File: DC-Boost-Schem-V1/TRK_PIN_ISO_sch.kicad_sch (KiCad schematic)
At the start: 10 parts, among them Q9 HCNR200-300E, U20 MCP6007, U21 MCP6007

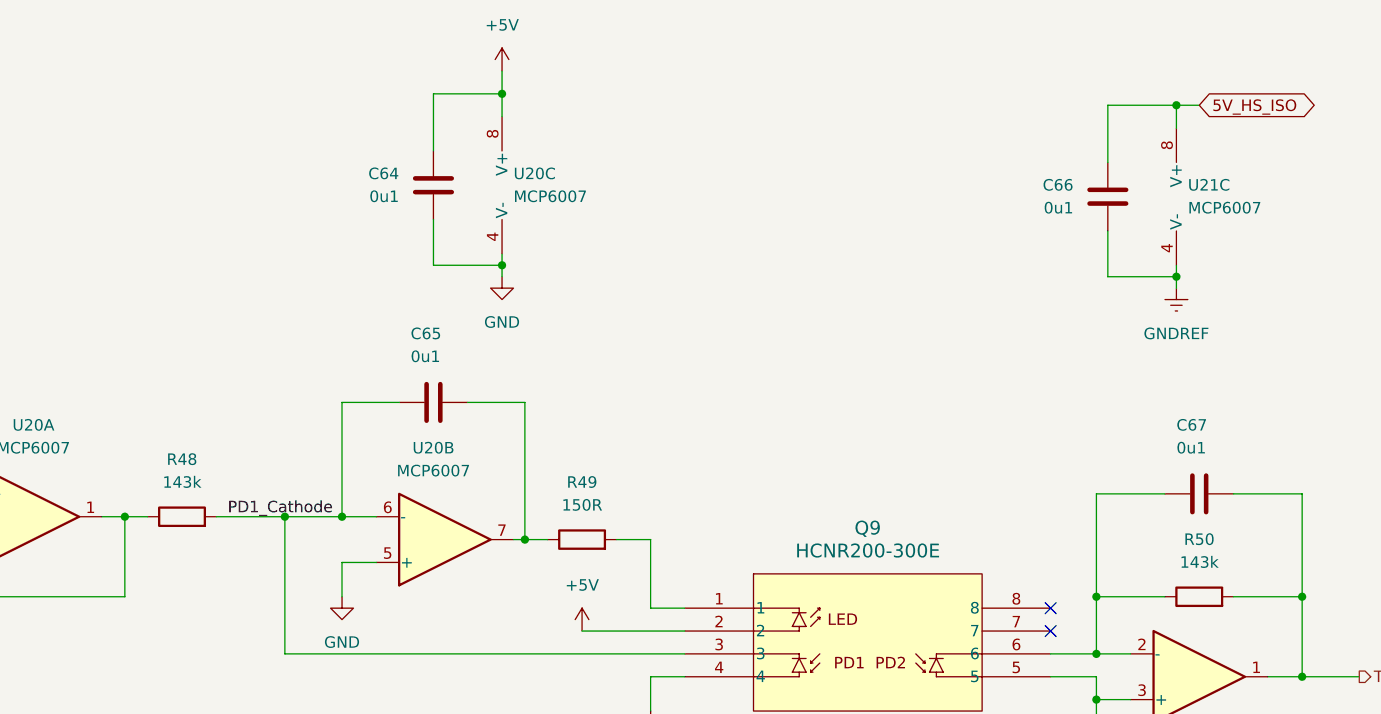
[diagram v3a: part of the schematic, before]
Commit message: More layout and routing
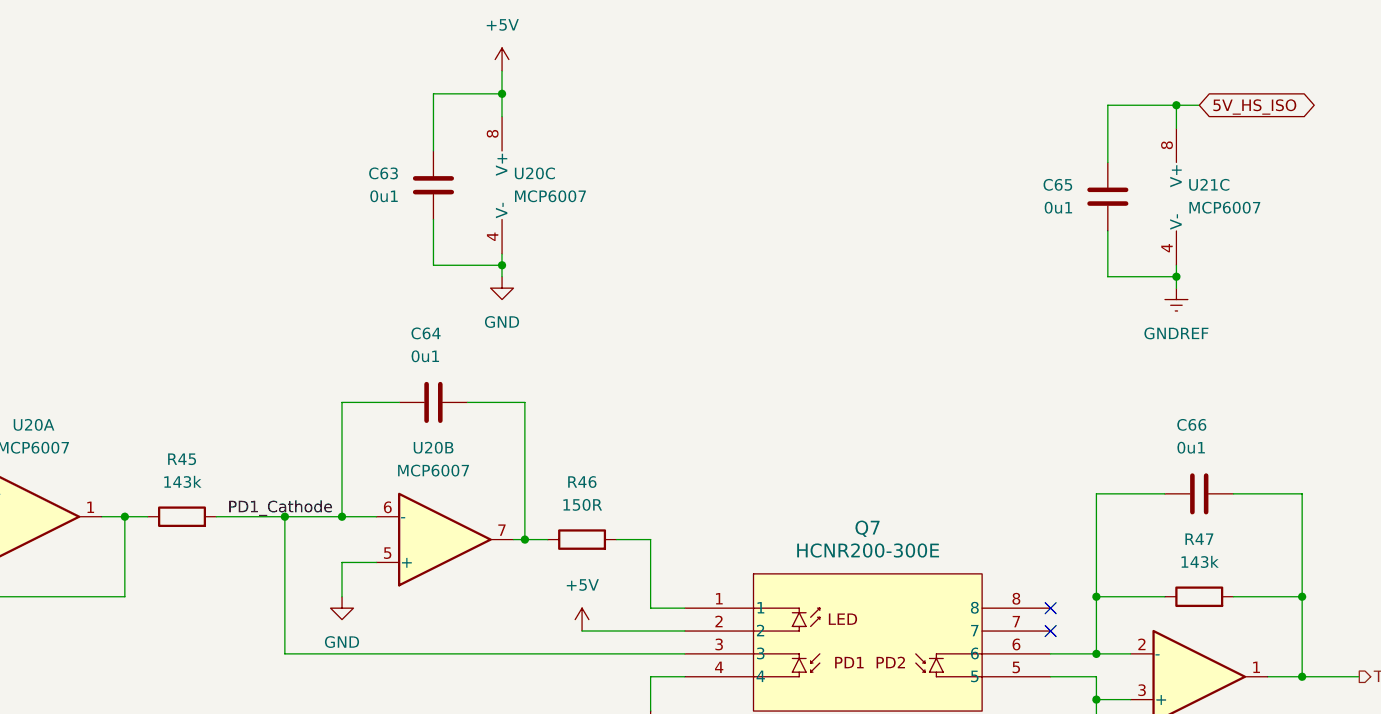
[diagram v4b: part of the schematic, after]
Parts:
- renumbered C64 to C63, C65 to C64, C66 to C65, C67 to C66, Q9 to Q7, R48 to R45, R49 to R46, R50 to R47
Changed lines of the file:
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@@
+		(dnp no)
+		(fields_autoplaced yes)
+		(property "Reference" "#PWR084"
+			(at 110.49 119.38 0)
+			(effects
+				(font
+					(size 1.27 1.27)
+				)
+				(hide yes)
+			)
+		)
+		(property "Value" "GND"
+			(at 110.49 118.11 0)
+			(effects
+				(font
+					(size 1.27 1.27)
+				)
+			)
+		)
+		(property "Footprint" ""
+			(at 110.49 113.03 0)
+			(effects
+				(font
+					(size 1.27 1.27)
+				)
+				(hide yes)
+			)
+		)
+		(property "Datasheet" ""
+			(at 110.49 113.03 0)
+			(effects
+				(font
+					(size 1.27 1.27)
+				)
+				(hide yes)
+			)
+		)
+		(property "Description" "Power symbol creates a global label with name \"GND\" , ground"
+			(at 110.49 113.03 0)
+			(effects
+				(font
+					(size 1.27 1.27)
+				)
+				(hide yes)
+			)
+		)
+		(pin "1"
+		)
+		(instances
+			(project "DC-DC-Boost-V1"
+				(path "/892bc44b-f7f8-4677-bf53-06d5523b6450/83854842-4c14-4e3d-b9f8-9c4b216ba0c1"
+					(reference "#PWR084")
+					(unit 1)
+				)
+			)
+		)
+	)
+	(symbol
+		(lib_id "power:GNDREF")
+		(at 203.2 78.74 0)
+		(unit 1)
+		(exclude_from_sim no)
+		(in_bom yes)
+		(on_board yes)
+		(dnp no)
+		(fields_autoplaced yes)
+		(property "Reference" "#PWR090"
+			(at 203.2 85.09 0)
+			(effects
+				(font
+					(size 1.27 1.27)
+				)
+				(hide yes)
+			)
+		)
+		(property "Value" "GNDREF"
+			(at 203.2 83.82 0)
+			(effects
+				(font
+					(size 1.27 1.27)
+				)
+			)
+		)
+		(property "Footprint" ""
+			(at 203.2 78.74 0)
+			(effects
+				(font
+					(size 1.27 1.27)
+				)
+				(hide yes)
+			)
+		)
+		(property "Datasheet" ""
+			(at 203.2 78.74 0)
+			(effects
+				(font
+					(size 1.27 1.27)
+				)
+				(hide yes)
+			)
+		)
+		(property "Description" "Power symbol creates a global label with name \"GNDREF\" , reference supply ground"
+			(at 203.2 78.74 0)
+			(effects
+				(font
+					(size 1.27 1.27)
+				)
+				(hide yes)
+			)
+		)
+		(pin "1"
+		)
+		(instances
+			(project "DC-DC-Boost-V1"
+				(path "/892bc44b-f7f8-4677-bf53-06d5523b6450/83854842-4c14-4e3d-b9f8-9c4b216ba0c1"
+					(reference "#PWR090")
+					(unit 1)
+				)
+			)
+		)
+	)
+	(symbol
+		(lib_id "power:GNDREF")
+		(at 194.31 129.54 0)
+		(unit 1)
+		(exclude_from_sim no)
+		(in_bom yes)
+		(on_board yes)
 		(dnp no)
 		(fields_autoplaced yes)
 		(property "Reference" "#PWR089"
-			(at 110.49 119.38 0)
-			(effects
-				(font
-					(size 1.27 1.27)
-				)
-				(hide yes)
-			)
-		)
-		(property "Value" "GND"
-			(at 110.49 118.11 0)
-			(effects
-				(font
-					(size 1.27 1.27)
-				)
-			)
-		)
-		(property "Footprint" ""
-			(at 110.49 113.03 0)
-			(effects
-				(font
-					(size 1.27 1.27)
-				)
-				(hide yes)
-			)
-		)
-		(property "Datasheet" ""
-			(at 110.49 113.03 0)
-			(effects
-				(font
-					(size 1.27 1.27)
-				)
-				(hide yes)
-			)
-		)
-		(property "Description" "Power symbol creates a global label with name \"GND\" , ground"
-			(at 110.49 113.03 0)
-			(effects
-				(font
-					(size 1.27 1.27)
-				)
-				(hide yes)
-			)
-		)
-		(pin "1"
-		)
-		(instances
-			(project "DC-DC-Boost-V1"
-				(path "/892bc44b-f7f8-4677-bf53-06d5523b6450/83854842-4c14-4e3d-b9f8-9c4b216ba0c1"
-					(reference "#PWR089")
-					(unit 1)
-				)
-			)
-		)
-	)
-	(symbol
-		(lib_id "power:GNDREF")
-		(at 203.2 78.74 0)
-		(unit 1)
-		(exclude_from_sim no)
-		(in_bom yes)
-		(on_board yes)
-		(dnp no)
-		(fields_autoplaced yes)
-		(property "Reference" "#PWR0601"
-			(at 203.2 85.09 0)
-			(effects
-				(font
-					(size 1.27 1.27)
-				)
-				(hide yes)
-			)
-		)
-		(property "Value" "GNDREF"
-			(at 203.2 83.82 0)
-			(effects
-				(font
-					(size 1.27 1.27)
-				)
-			)
-		)
-		(property "Footprint" ""
-			(at 203.2 78.74 0)
-			(effects
-				(font
-					(size 1.27 1.27)
-				)
-				(hide yes)
-			)
-		)
-		(property "Datasheet" ""
-			(at 203.2 78.74 0)
-			(effects
-				(font
-					(size 1.27 1.27)
-				)
-				(hide yes)
-			)
-		)
-		(property "Description" "Power symbol creates a global label with name \"GNDREF\" , reference supply ground"
-			(at 203.2 78.74 0)
-			(effects
-				(font
-					(size 1.27 1.27)
-				)
-				(hide yes)
-			)
-		)
-		(pin "1"
-		)
-		(instances
-			(project "DC-DC-Boost-V1"
-				(path "/892bc44b-f7f8-4677-bf53-06d5523b6450/83854842-4c14-4e3d-b9f8-9c4b216ba0c1"
-					(reference "#PWR0601")
-					(unit 1)
-				)
-			)
-		)
-	)
-	(symbol
-		(lib_id "power:GNDREF")
-		(at 194.31 129.54 0)
-		(unit 1)
-		(exclude_from_sim no)
-		(in_bom yes)
-		(on_board yes)
-		(dnp no)
-		(fields_autoplaced yes)
-		(property "Reference" "#PWR0602"
 			(at 194.31 135.89 0)
 			(effects
@@
 			(project "DC-DC-Boost-V1"
 				(path "/892bc44b-f7f8-4677-bf53-06d5523b6450/83854842-4c14-4e3d-b9f8-9c4b216ba0c1"
-					(reference "#PWR0602")
+					(reference "#PWR089")
 					(unit 1)
 				)
@@
 		(dnp no)
 		(fields_autoplaced yes)
-		(property "Reference" "R50"
+		(property "Reference" "R47"
 			(at 205.74 106.68 90)
 			(effects
@@
 			(project "DC-DC-Boost-V1"
 				(path "/892bc44b-f7f8-4677-bf53-06d5523b6450/83854842-4c14-4e3d-b9f8-9c4b216ba0c1"
-					(reference "R50")
+					(reference "R47")
 					(unit 1)
 				)
@@
 		(dnp no)
 		(fields_autoplaced yes)
-		(property "Reference" "#PWR090"
+		(property "Reference" "#PWR086"
 			(at 128.27 83.82 0)
 			(effects
@@
 			(project "DC-DC-Boost-V1"
 				(path "/892bc44b-f7f8-4677-bf53-06d5523b6450/83854842-4c14-4e3d-b9f8-9c4b216ba0c1"
-					(reference "#PWR090")
+					(reference "#PWR086")
 					(unit 1)
 				)
@@
 		(on_board yes)
 		(dnp no)
-		(property "Reference" "C64"
+		(property "Reference" "C63"
 			(at 116.84 66.04 0)
 			(effects
@@
 			(project "DC-DC-Boost-V1"
 				(path "/892bc44b-f7f8-4677-bf53-06d5523b6450/83854842-4c14-4e3d-b9f8-9c4b216ba0c1"
-					(reference "C64")
+					(reference "C63")
 					(unit 1)
 				)
@@
 		(on_board yes)
 		(dnp no)
-		(property "Reference" "C67"
+		(property "Reference" "C66"
 			(at 203.2 93.98 90)
 			(effects
@@
 			(project "DC-DC-Boost-V1"
 				(path "/892bc44b-f7f8-4677-bf53-06d5523b6450/83854842-4c14-4e3d-b9f8-9c4b216ba0c1"
-					(reference "C67")
+					(reference "C66")
 					(unit 1)
 				)
@@
 		(dnp no)
 		(fields_autoplaced yes)
-		(property "Reference" "R48"
+		(property "Reference" "R45"
 			(at 92.71 97.79 90)
 			(effects
@@
 			(project "DC-DC-Boost-V1"
 				(path "/892bc44b-f7f8-4677-bf53-06d5523b6450/83854842-4c14-4e3d-b9f8-9c4b216ba0c1"
-					(reference "R48")
+					(reference "R45")
 					(unit 1)
 				)
@@
 		(dnp no)
 		(fields_autoplaced yes)
-		(property "Reference" "#PWR093"
+		(property "Reference" "#PWR088"
 			(at 144.78 132.08 0)
 			(effects
@@
 			(project "DC-DC-Boost-V1"
 				(path "/892bc44b-f7f8-4677-bf53-06d5523b6450/83854842-4c14-4e3d-b9f8-9c4b216ba0c1"
-					(reference "#PWR093")
+					(reference "#PWR088")
 					(unit 1)
 				)
@@
 		(dnp no)
 		(fields_autoplaced yes)
-		(property "Reference" "#PWR092"
+		(property "Reference" "#PWR087"
 			(at 137.16 120.65 0)
 			(effects
@@
 			(project "DC-DC-Boost-V1"
 				(path "/892bc44b-f7f8-4677-bf53-06d5523b6450/83854842-4c14-4e3d-b9f8-9c4b216ba0c1"
-					(reference "#PWR092")
+					(reference "#PWR087")
 					(unit 1)
 				)
@@
 		(on_board yes)
 		(dnp no)
-		(property "Reference" "Q9"
+		(property "Reference" "Q7"
 			(at 168.91 105.41 0)
 			(effects
@@
 			(project "DC-DC-Boost-V1"
 				(path "/892bc44b-f7f8-4677-bf53-06d5523b6450/83854842-4c14-4e3d-b9f8-9c4b216ba0c1"
-					(reference "Q9")
+					(reference "Q7")
 					(unit 1)
 				)
@@
 		(dnp no)
 		(fields_autoplaced yes)
-		(property "Reference" "R49"
+		(property "Reference" "R46"
 			(at 137.16 100.33 90)
 			(effects
@@
 			(project "DC-DC-Boost-V1"
 				(path "/892bc44b-f7f8-4677-bf53-06d5523b6450/83854842-4c14-4e3d-b9f8-9c4b216ba0c1"
-					(reference "R49")
+					(reference "R46")
 					(unit 1)
 				)
@@
 		(dnp no)
 		(fields_autoplaced yes)
-		(property "Reference" "#PWR091"
+		(property "Reference" "#PWR085"
 			(at 128.27 58.42 0)
 			(effects
@@
 			(project "DC-DC-Boost-V1"
 				(path "/892bc44b-f7f8-4677-bf53-06d5523b6450/83854842-4c14-4e3d-b9f8-9c4b216ba0c1"
-					(reference "#PWR091")
+					(reference "#PWR085")
 					(unit 1)
 				)
@@
 		(on_board yes)
 		(dnp no)
-		(property "Reference" "C65"
+		(property "Reference" "C64"
 			(at 118.11 83.82 90)
 			(effects
@@
 			(project "DC-DC-Boost-V1"
 				(path "/892bc44b-f7f8-4677-bf53-06d5523b6450/83854842-4c14-4e3d-b9f8-9c4b216ba0c1"
-					(reference "C65")
+					(reference "C64")
 					(unit 1)
 				)
@@
 		(on_board yes)
 		(dnp no)
-		(property "Reference" "C66"
+		(property "Reference" "C65"
 			(at 191.77 67.31 0)
 			(effects
@@
 			(project "DC-DC-Boost-V1"
 				(path "/892bc44b-f7f8-4677-bf53-06d5523b6450/83854842-4c14-4e3d-b9f8-9c4b216ba0c1"
-					(reference "C66")
-					(unit 1)
-				)
+					(reference "C65")
+					(unit 1)
+				)

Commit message: Added more to layout
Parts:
- renumbered C63 to C66, C64 to C67, C65 to C68, C66 to C69, R45 to R47, R46 to R48, R47 to R49
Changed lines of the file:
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@@
 		(dnp no)
 		(fields_autoplaced yes)
-		(property "Reference" "R47"
+		(property "Reference" "R49"
 			(at 205.74 106.68 90)
 			(effects
@@
 			(project "DC-DC-Boost-V1"
 				(path "/892bc44b-f7f8-4677-bf53-06d5523b6450/83854842-4c14-4e3d-b9f8-9c4b216ba0c1"
-					(reference "R47")
+					(reference "R49")
 					(unit 1)
 				)
@@
 		(on_board yes)
 		(dnp no)
-		(property "Reference" "C63"
+		(property "Reference" "C66"
 			(at 116.84 66.04 0)
 			(effects
@@
 			(project "DC-DC-Boost-V1"
 				(path "/892bc44b-f7f8-4677-bf53-06d5523b6450/83854842-4c14-4e3d-b9f8-9c4b216ba0c1"
-					(reference "C63")
+					(reference "C66")
 					(unit 1)
 				)
@@
 		(on_board yes)
 		(dnp no)
-		(property "Reference" "C66"
+		(property "Reference" "C69"
 			(at 203.2 93.98 90)
 			(effects
@@
 			(project "DC-DC-Boost-V1"
 				(path "/892bc44b-f7f8-4677-bf53-06d5523b6450/83854842-4c14-4e3d-b9f8-9c4b216ba0c1"
-					(reference "C66")
+					(reference "C69")
 					(unit 1)
 				)
@@
 		(dnp no)
 		(fields_autoplaced yes)
-		(property "Reference" "R45"
+		(property "Reference" "R47"
 			(at 92.71 97.79 90)
 			(effects
@@
 			(project "DC-DC-Boost-V1"
 				(path "/892bc44b-f7f8-4677-bf53-06d5523b6450/83854842-4c14-4e3d-b9f8-9c4b216ba0c1"
-					(reference "R45")
+					(reference "R47")
 					(unit 1)
 				)
@@
 		(dnp no)
 		(fields_autoplaced yes)
-		(property "Reference" "R46"
+		(property "Reference" "R48"
 			(at 137.16 100.33 90)
 			(effects
@@
 			(project "DC-DC-Boost-V1"
 				(path "/892bc44b-f7f8-4677-bf53-06d5523b6450/83854842-4c14-4e3d-b9f8-9c4b216ba0c1"
-					(reference "R46")
+					(reference "R48")
 					(unit 1)
 				)
@@
 		(on_board yes)
 		(dnp no)
-		(property "Reference" "C64"
+		(property "Reference" "C67"
 			(at 118.11 83.82 90)
 			(effects
@@
 			(project "DC-DC-Boost-V1"
 				(path "/892bc44b-f7f8-4677-bf53-06d5523b6450/83854842-4c14-4e3d-b9f8-9c4b216ba0c1"
-					(reference "C64")
+					(reference "C67")
 					(unit 1)
 				)
@@
 		(on_board yes)
 		(dnp no)
-		(property "Reference" "C65"
+		(property "Reference" "C68"
 			(at 191.77 67.31 0)
 			(effects
@@
 			(project "DC-DC-Boost-V1"
 				(path "/892bc44b-f7f8-4677-bf53-06d5523b6450/83854842-4c14-4e3d-b9f8-9c4b216ba0c1"
-					(reference "C65")
-					(unit 1)
-				)
+					(reference "C68")
+					(unit 1)
+				)
